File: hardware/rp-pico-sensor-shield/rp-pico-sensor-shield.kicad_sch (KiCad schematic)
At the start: 42 parts, among them J1 Barrel_Jack, J10 Conn_01x04, J11 Conn_01x04, J12 Conn_01x04, J13 Conn_01x04, J14 Conn_01x04, J15 Conn_01x04, J16 Conn_01x04, J17 Conn_01x03, J18 Conn_01x03, J19 Conn_01x03, J2 Conn_01x04, J20 Conn_01x03, J21 Conn_01x03, J22 Conn_01x03, J23 Conn_01x04, J24 Screw Terminal, J25 Conn_01x04, J26 I2C0, J27 I2C1, J28 AGND, J29 Conn_01x03, J3 Conn_01x04, J30 Conn_01x03, J4 Conn_01x04, J5 Conn_01x04, J6 Conn_01x04, J7 Conn_01x04, J8 Conn_01x04, J9 Conn_01x04, Q1 DMG2305UX, SW1 SW_Push, U1 NCP1117-5.0_SOT223, U2 Pico

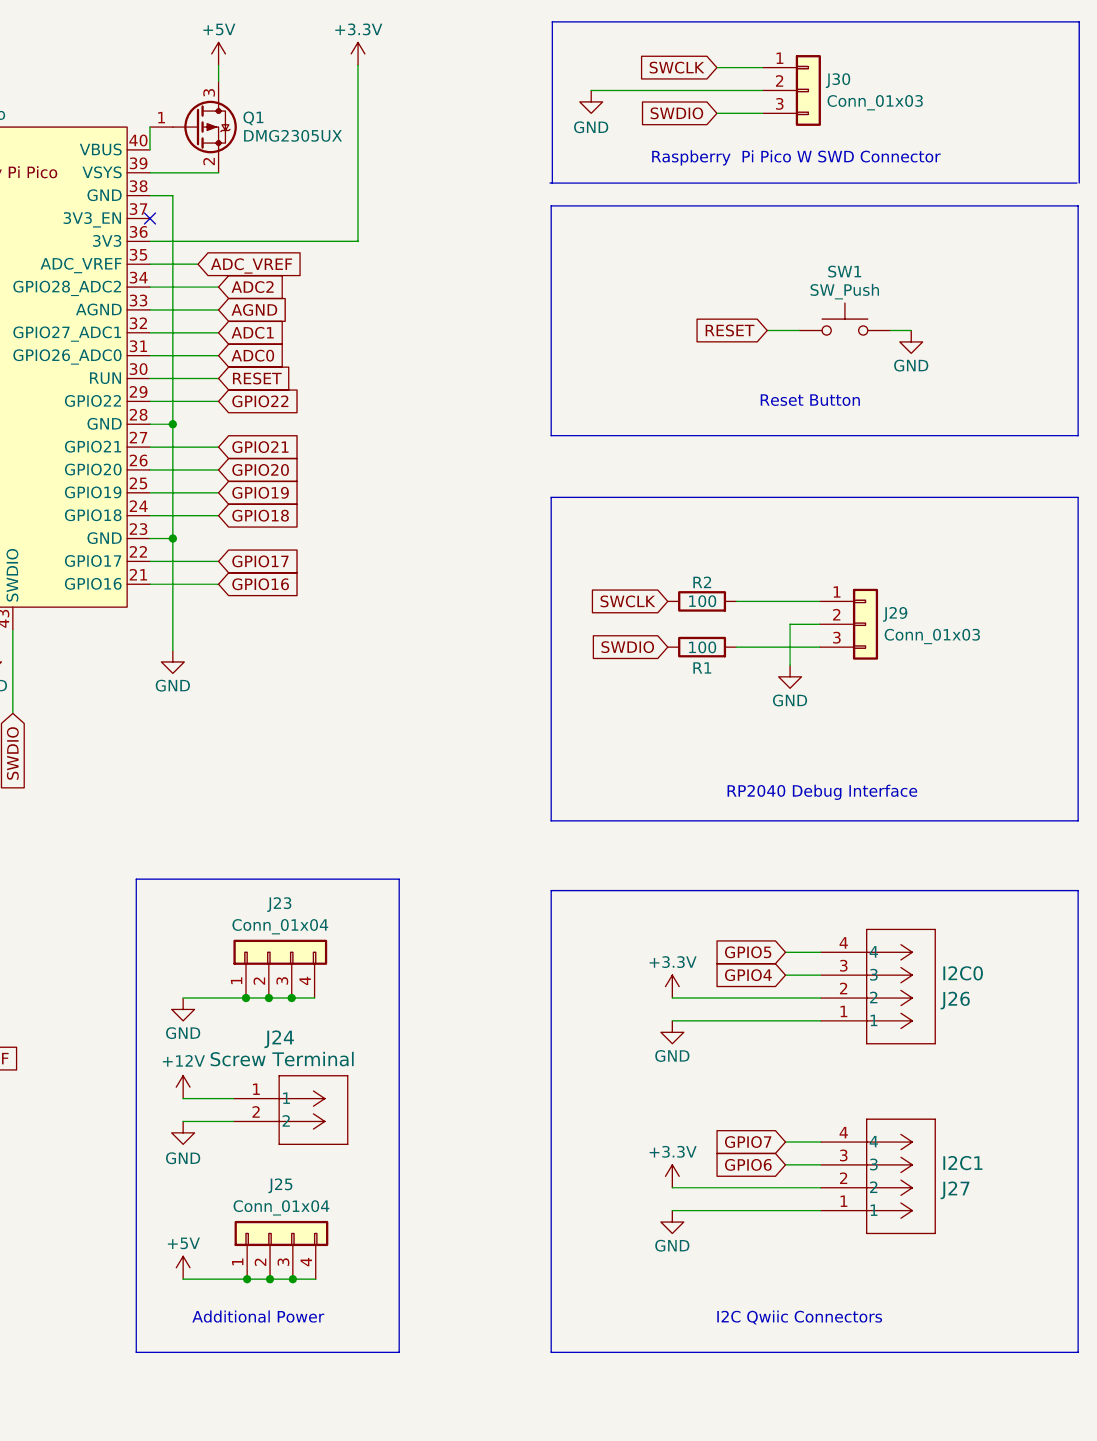
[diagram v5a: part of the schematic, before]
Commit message: serperated I2C busses for display and gyro
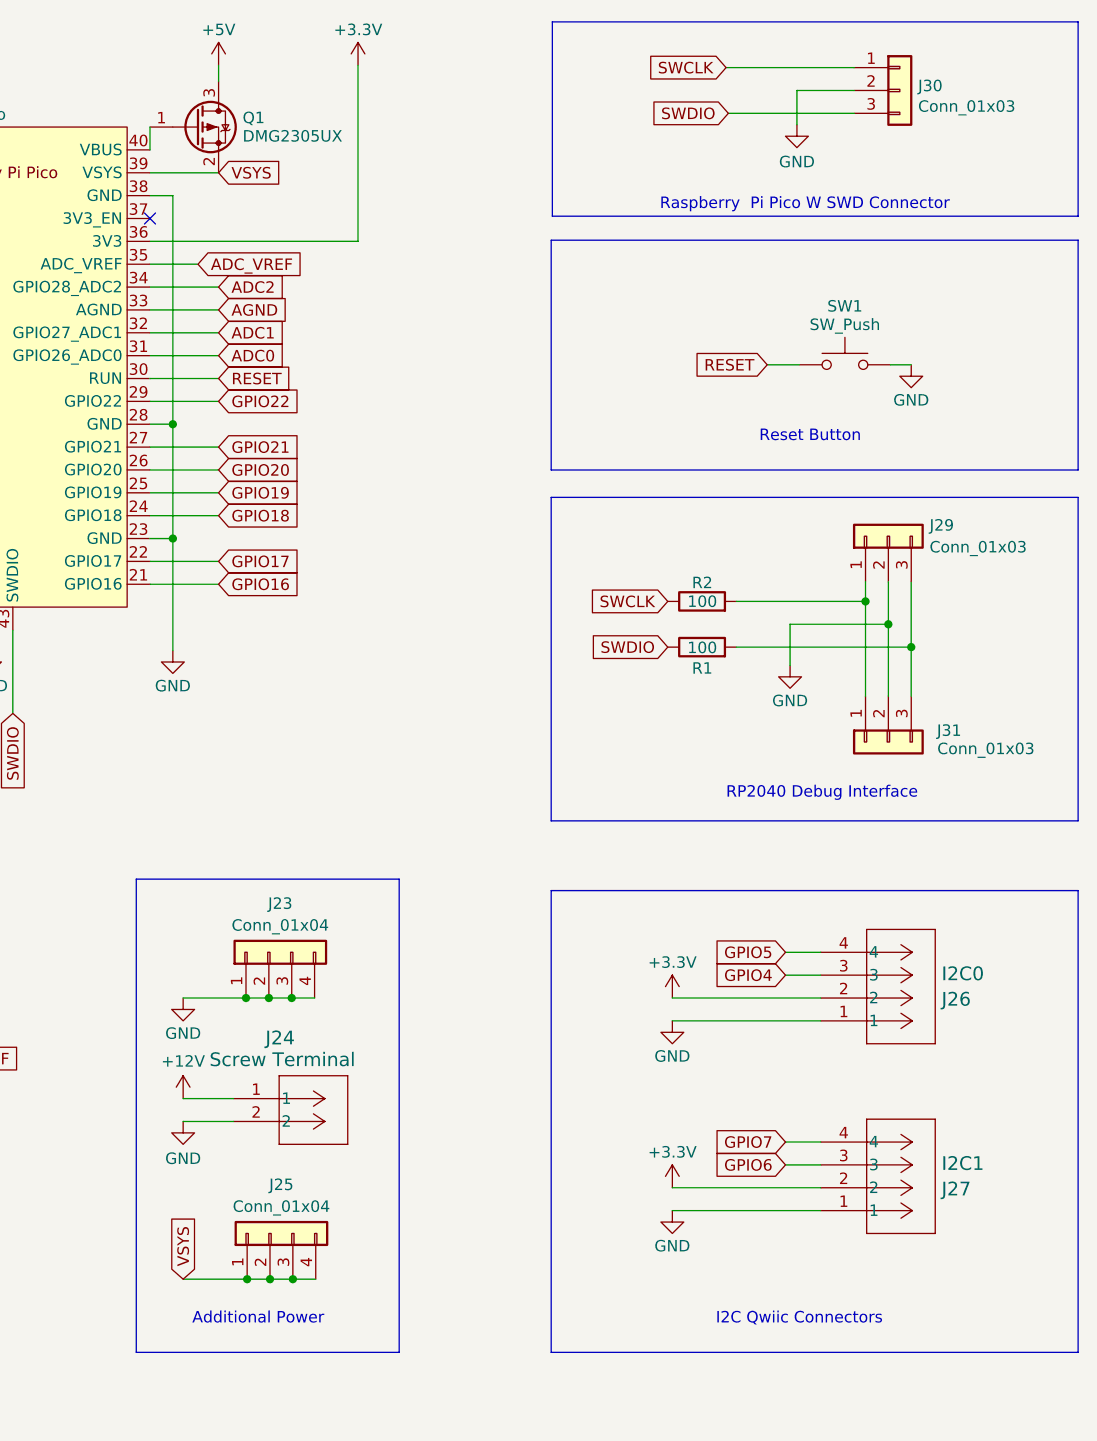
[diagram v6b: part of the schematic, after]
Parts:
- added J31: Conn_01x03, Connector_PinHeader_2.54mm:PinHeader_1x03_P2.54mm_Horizontal, symbol Connector_Generic:Conn_01x03
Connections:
- net +5V: no longer J25.1 (Pin_1), J25.2 (Pin_2), J25.3 (Pin_3), J25.4 (Pin_4)
- net GND: now also J31.2 (Pin_2)
- net VSYS: now reaches Q1.2 (S), U2.39 (VSYS)
- net VSYS: now also J25.1 (Pin_1), J25.2 (Pin_2), J25.3 (Pin_3), J25.4 (Pin_4)
- net at J29.1 (Pin_1), R2.2: now also J31.1 (Pin_1)
- net at J29.3 (Pin_3), R1.2: now also J31.3 (Pin_3)
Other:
- moved on the sheet: J29, J30, SW1
